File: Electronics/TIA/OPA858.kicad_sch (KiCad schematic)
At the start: 3 parts, among them U1 ${SIM.PARAMS}

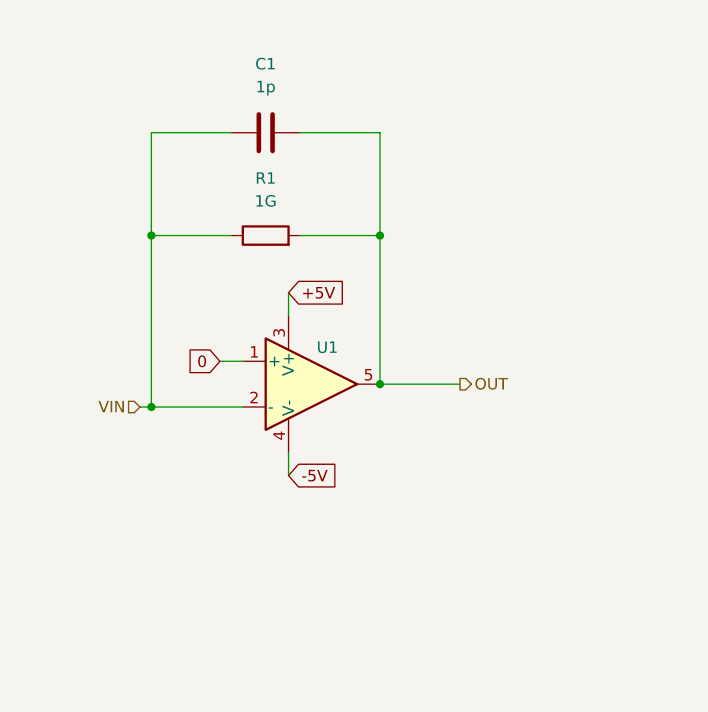
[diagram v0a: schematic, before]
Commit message: Create a robust TIA design following the requirements
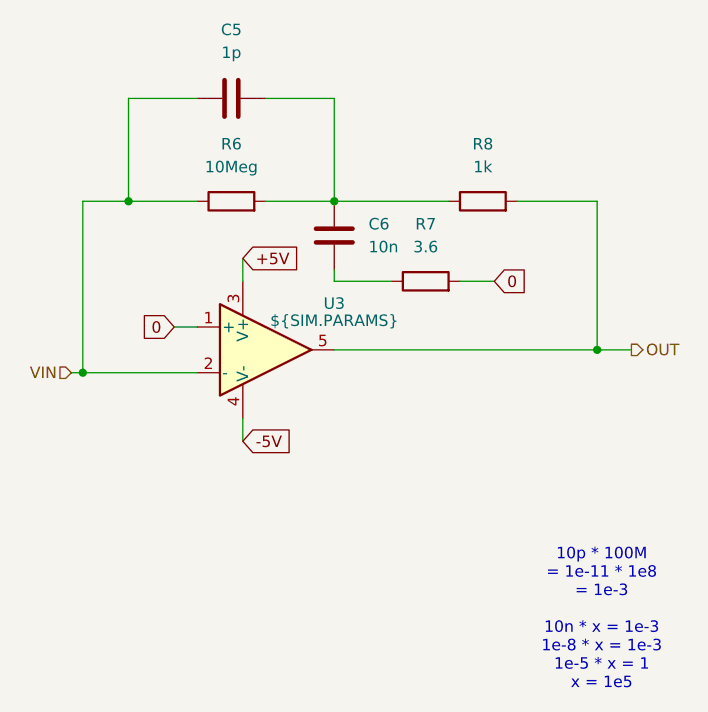
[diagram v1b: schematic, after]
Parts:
- removed C1: 1p, symbol Device:C
- removed R1: 1G, symbol Device:R
- removed U1: ${SIM.PARAMS}, symbol Simulation_SPICE:OPAMP
- added C5: 1p, symbol Device:C
- added C6: 10n, symbol Device:C
- added R6: 10Meg, symbol Device:R
- added R7: 3.6, symbol Device:R
- added R8: 1k, symbol Device:R
- added U3: ${SIM.PARAMS}, symbol Simulation_SPICE:OPAMP
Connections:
- net +5V: now also U3.3 (V+)
- net -5V: now also U3.4 (V-)
- net 0: now also R7.2, U3.1 (+)
- net OUT: now also R8.2, U3.5
- net VIN: now also C5.1, R6.1, U3.2 (-)
- new net: C5.2, C6.2, R6.2, R8.1
- new net: C6.1, R7.1
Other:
- note added: "10p * 100M = 1e-11 * 1e8 = 1e-3 10n * x = 1e-3 1e-8 * x = 1e-3 1e-5 * x = 1 x = 1e5"

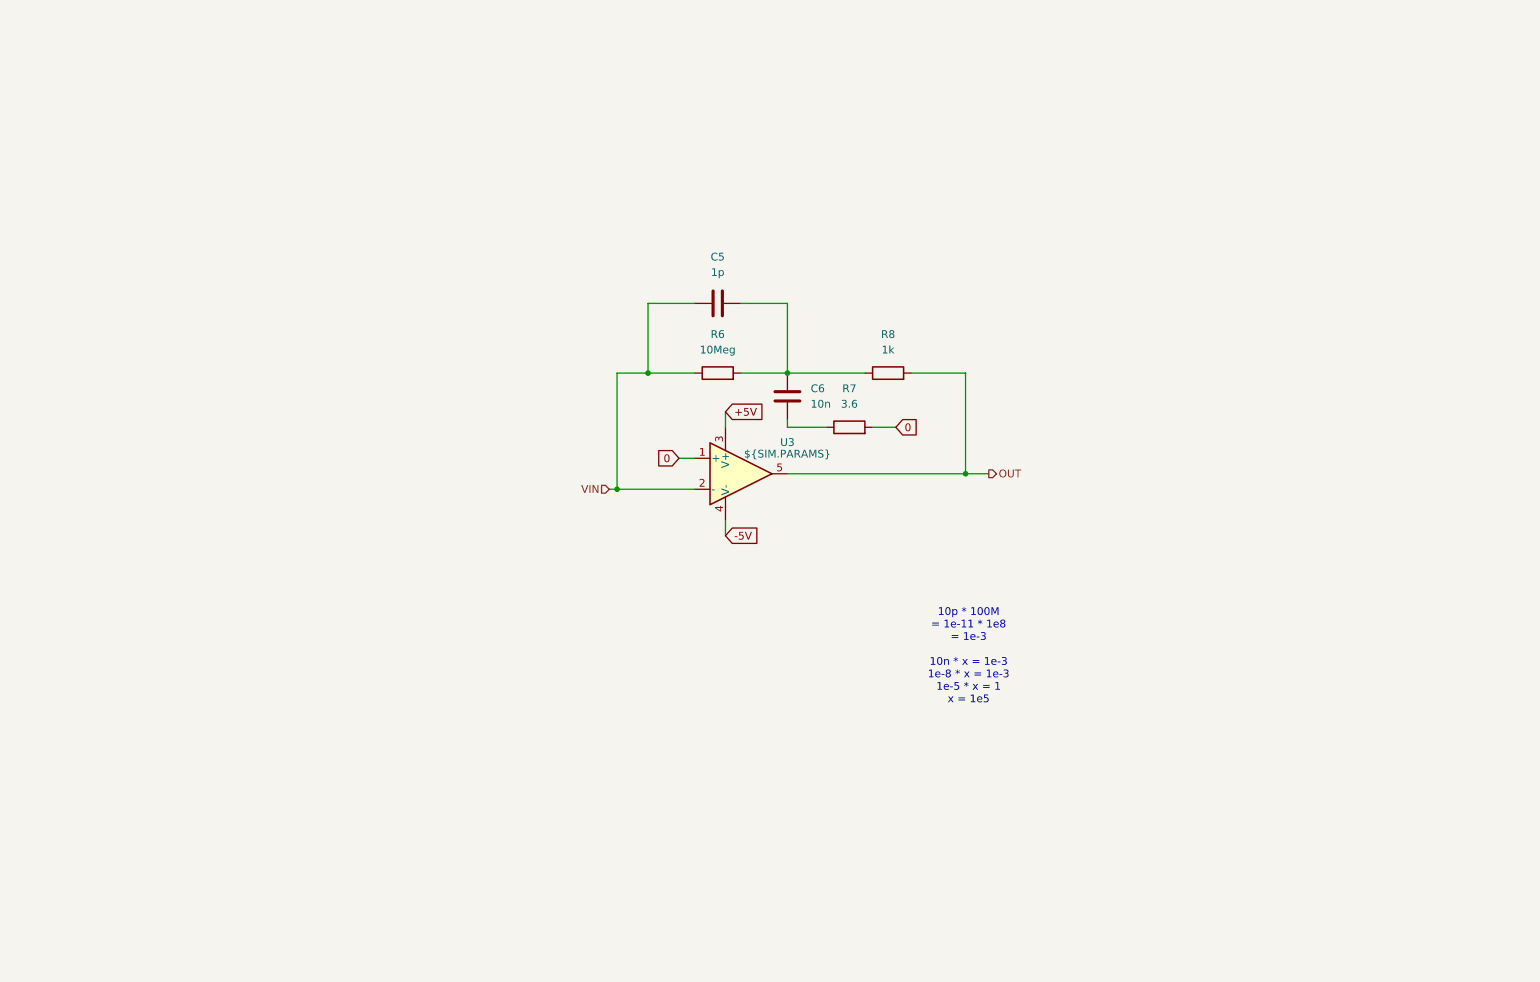
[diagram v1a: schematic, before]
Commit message: Create simpler stability simulation
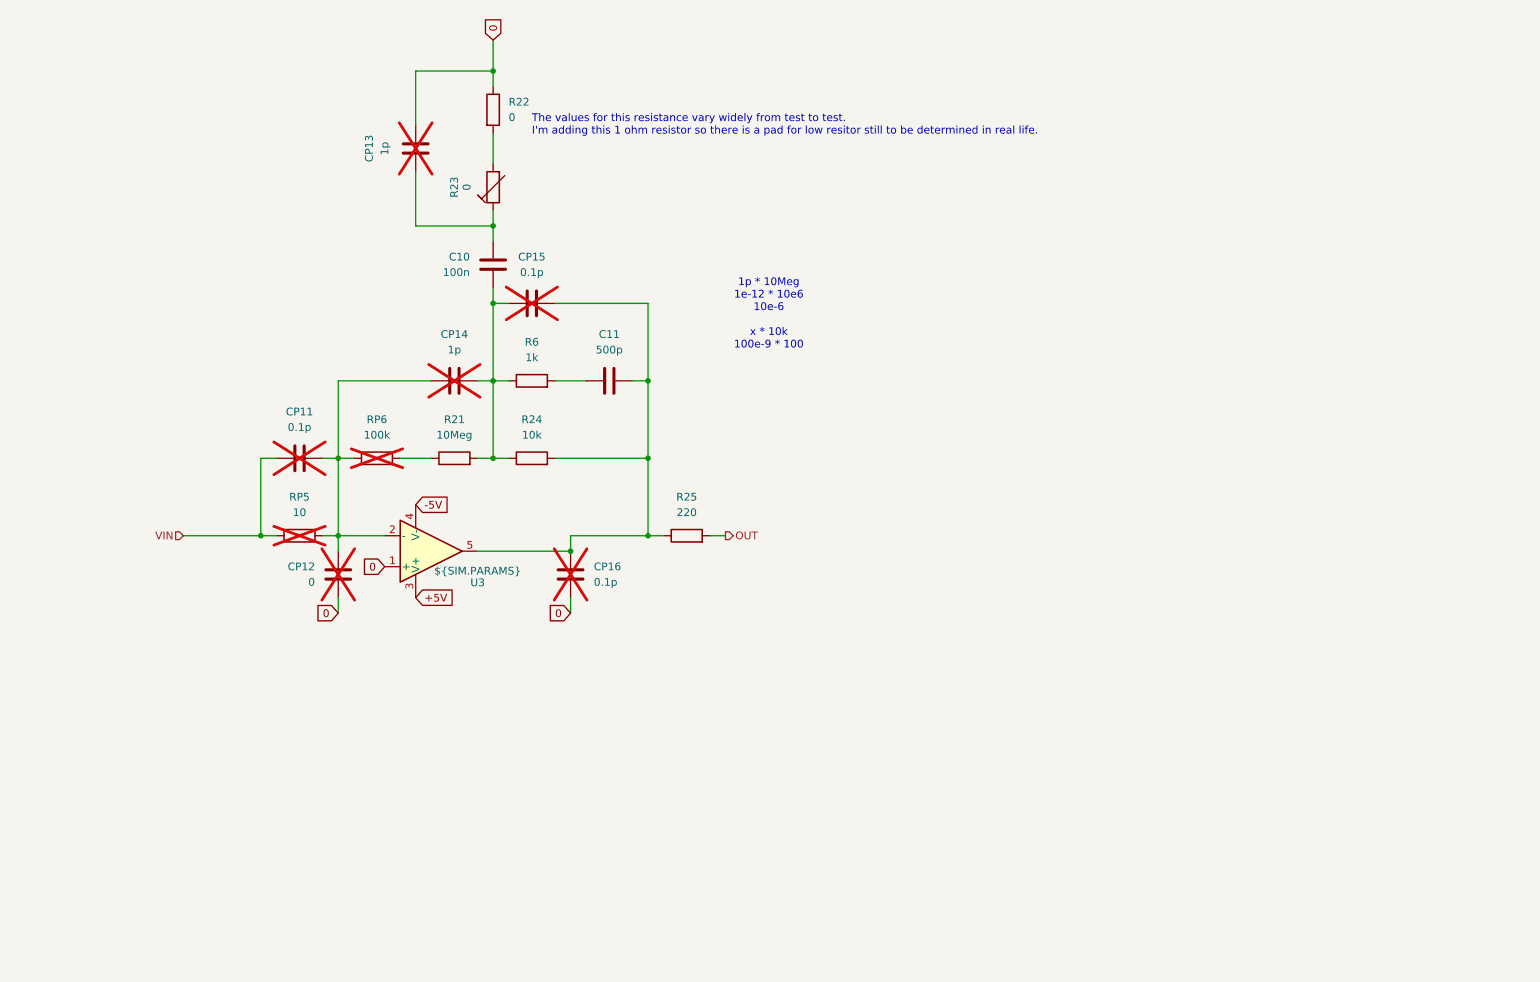
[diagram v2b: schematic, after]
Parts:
- removed C5: 1p, symbol Device:C
- removed C6: 10n, symbol Device:C
- removed R7: 3.6, symbol Device:R
- removed R8: 1k, symbol Device:R
- added C10: 100n, symbol Device:C
- added C11: 500p, symbol Device:C
- added CP11, CP15, CP16: 0.1p, symbol Device:C
- added CP12: 0, symbol Device:C
- added CP13, CP14: 1p, symbol Device:C
- added R21: 10Meg, symbol Device:R
- added R22: 0, symbol Device:R
- added R23: 0, symbol Device:R_Trim
- added R24: 10k, symbol Device:R
- added R25: 220, symbol Device:R
- added RP5: 10, symbol Device:R
- added RP6: 100k, symbol Device:R
- R6: value 10Meg -> 1k
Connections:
- net 0: now also CP12.2, CP13.2, CP16.1, R22.1
- net OUT: now also R25.2; no longer U3.5
- net VIN: now also CP11.1, RP5.1; no longer R6.1, U3.2 (-)
- net at R6.2: now also C11.1
- new net: C10.2, CP14.1, CP15.1, R21.2, R24.1, R6.1
- new net: C11.2, CP15.2, CP16.2, R24.2, R25.1, U3.5
- new net: C10.1, CP13.1, R23.1
- new net: CP11.2, CP12.1, CP14.2, RP5.2, RP6.1, U3.2 (-)
- new net: R21.1, RP6.2
- new net: R22.2, R23.2
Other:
- note added: "1p * 10Meg 1e-12 * 10e6 10e-6 x * 10k 100e-9 * 100"
- note added: "The values for this resistance vary widely from test to test. I'm adding this 1 ohm resistor so there is a pad for low resitor still to be determined in real life."
- note removed: "10p * 100M = 1e-11 * 1e8 = 1e-3 10n * x = 1e-3 1e-8 * x = 1e-3 1e-5 * x = 1 x = 1e5"
- moved on the sheet: U3

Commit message: Remove old simulations
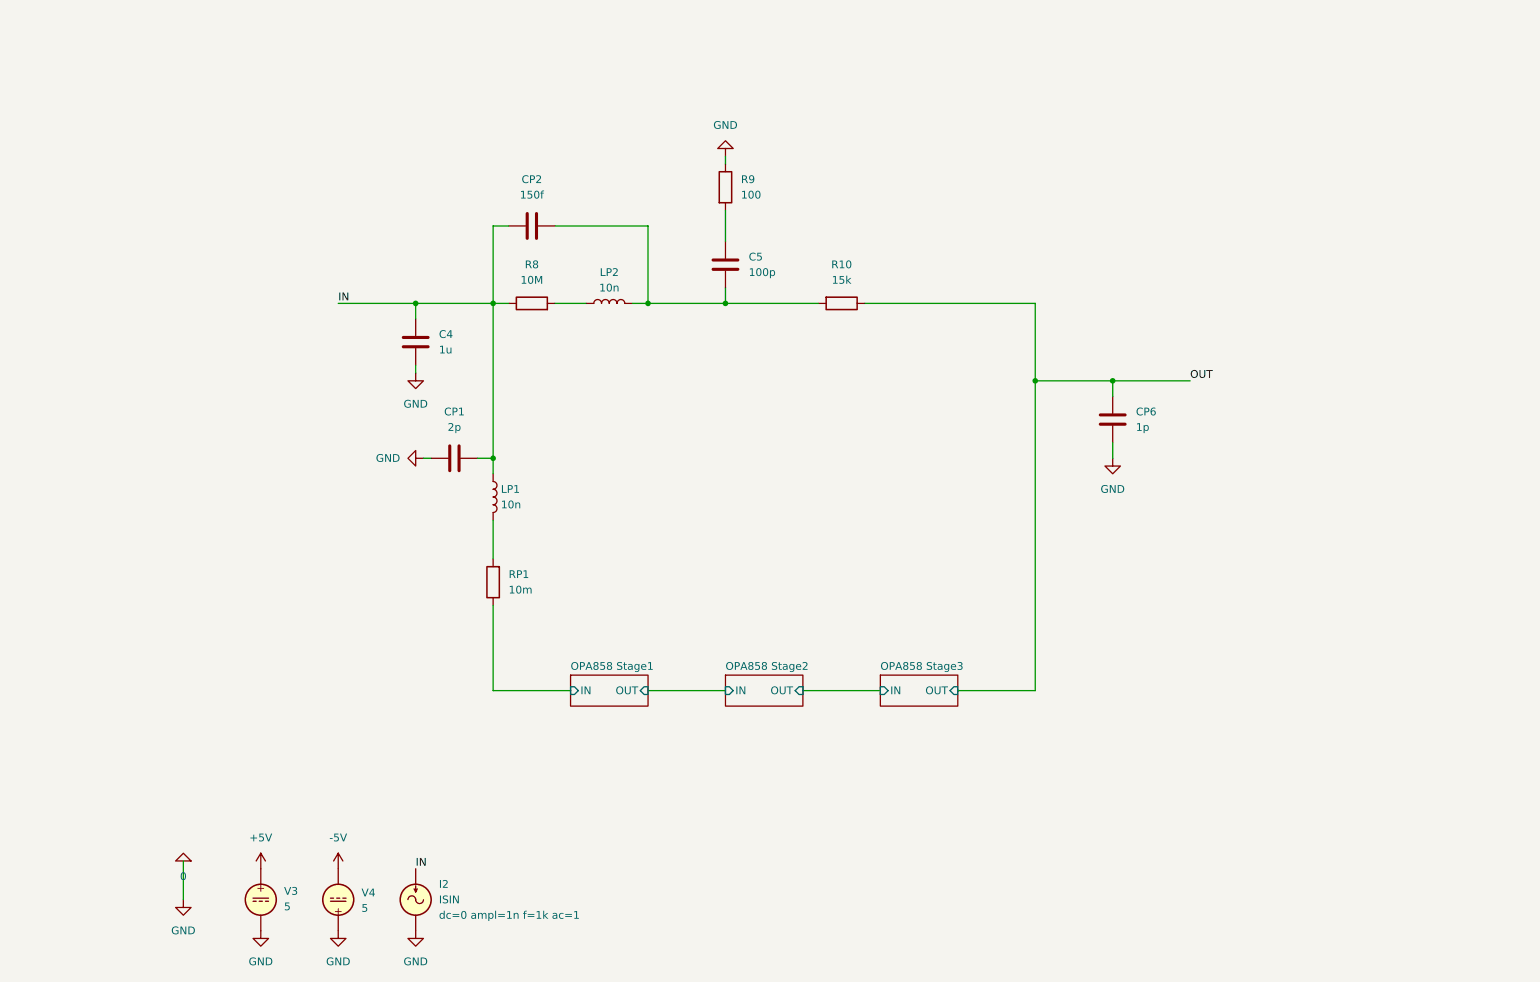
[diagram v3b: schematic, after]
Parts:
- removed C10: 100n, symbol Device:C
- removed C11: 500p, symbol Device:C
- removed CP11, CP15, CP16: 0.1p, symbol Device:C
- removed CP12: 0, symbol Device:C
- removed CP13, CP14: 1p, symbol Device:C
- removed R21: 10Meg, symbol Device:R
- removed R22: 0, symbol Device:R
- removed R23: 0, symbol Device:R_Trim
- removed R24: 10k, symbol Device:R
- removed R25: 220, symbol Device:R
- removed R6: 1k, symbol Device:R
- removed RP5: 10, symbol Device:R
- removed RP6: 100k, symbol Device:R
- removed U3: ${SIM.PARAMS}, symbol Simulation_SPICE:OPAMP
- added C4: 1u, symbol Device:C
- added C5: 100p, symbol Device:C
- added CP1: 2p, symbol Device:C
- added CP2: 150f, symbol Device:C
- added CP6: 1p, symbol Device:C
- added I2: ISIN, symbol Simulation_SPICE:ISIN
- added LP1, LP2: 10n, symbol Device:L
- added R10: 15k, symbol Device:R
- added R8: 10M, symbol Device:R
- added R9: 100, symbol Device:R
- added RP1: 10m, symbol Device:R
- added V3, V4: 5, symbol Simulation_SPICE:VDC
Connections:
- net +5V: now also V3.1
- net -5V: now also V4.2
- net 0: now also C4.2, CP1.2, CP6.1, I2.2, R9.1, V3.2, V4.1
- net OUT: now also CP6.2, R10.1
- new net: C5.2, CP2.2, LP2.2, R10.2
- new net: LP1.2, RP1.2
- new net: C5.1, R9.2
- new net: LP2.1, R8.2
- new net IN: C4.1, CP1.1, CP2.1, I2.1, LP1.1, R8.1
- new net OPA858 Stage1/IN: RP1.1
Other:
- added sheet OPA858 Stage1 (OPA858 Stage.kicad_sch)
- added sheet OPA858 Stage2 (OPA858 Stage.kicad_sch)
- added sheet OPA858 Stage3 (OPA858 Stage.kicad_sch)
- note removed: "1p * 10Meg 1e-12 * 10e6 10e-6 x * 10k 100e-9 * 100"
- note removed: "The values for this resistance vary widely from test to test. I'm adding this 1 ohm resistor so there is a pad for low resitor still to be determined in real life."

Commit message: Mess around with the simulation
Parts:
- removed CP6: 1p, symbol Device:C
- added C8: 100f, symbol Device:C
- added C9: 1f, symbol Device:C
- added V7: VSIN, symbol Simulation_SPICE:VSIN
- C6: renamed from C4; value 1u -> 1f
- C7: renamed from C5; value 100p -> 1n
- R13: renamed from R9; value 100 -> 1m
- R14: renamed from R10; value 15k -> 1.5k
- renumbered R8 to R12
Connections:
- net 0: now also C9.2, V7.2
- net IN: now also V7.1
- net OUT: now also C8.2, C9.1
- net at C7.2, CP2.2, LP2.2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: now also C8.1
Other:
- note added: "10M * 150f 10E6 * 150E-15 1E7 * 1.5E-13 1.5E-6 1.5k * 1n 1.5E3 * 1E-9 1.5E-6"
- moved on the sheet: C6, C7, CP1, CP2, I2, LP1, LP2, R12, R13, R14, RP1, V3
